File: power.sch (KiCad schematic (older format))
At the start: 19 parts, among them SW5 SW_DPST_NKK_M2021, U13 LM317_SOT223_4pin, U14 LM317_SOT223_4pin

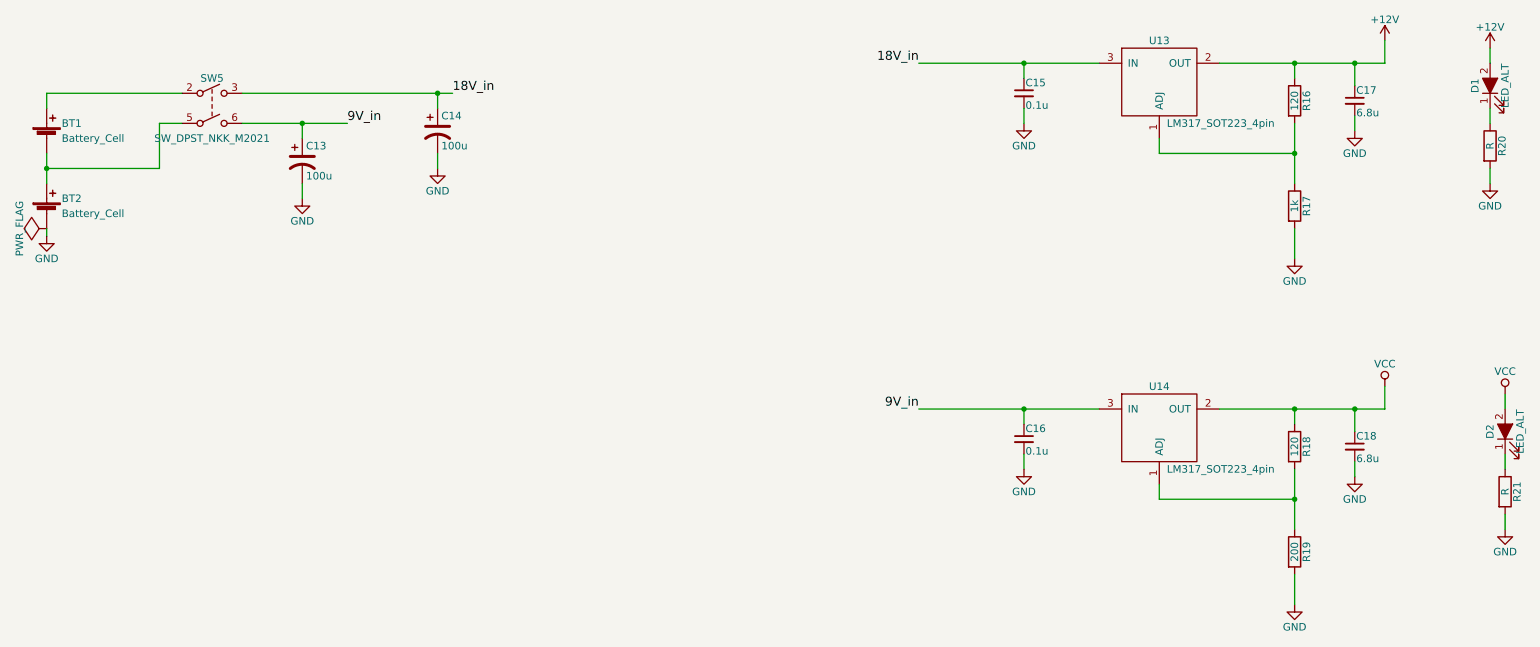
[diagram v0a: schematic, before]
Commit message: Added testpoints for VCC, 12V, and GND
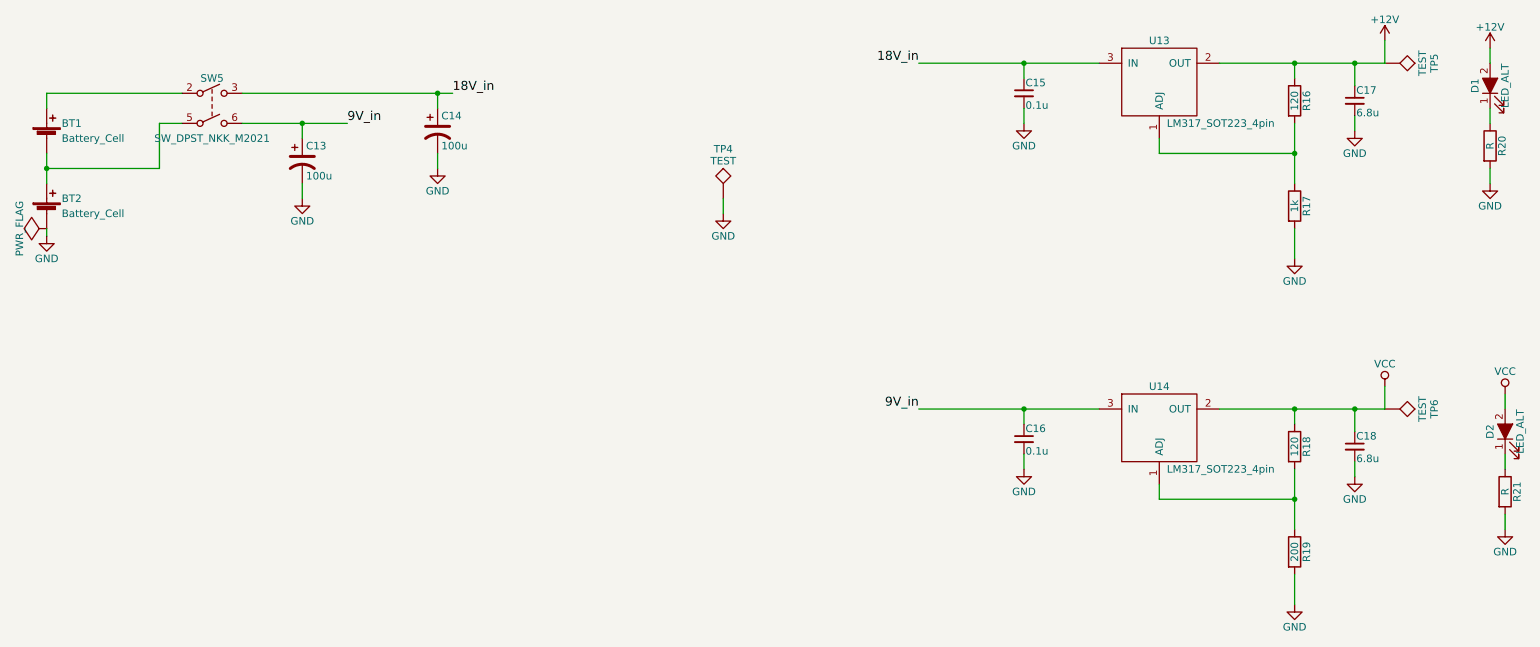
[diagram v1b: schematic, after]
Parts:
- added TP4, TP5, TP6: TEST, Measurement_Points:Measurement_Point_Square-TH_Big, symbol TEST
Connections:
- net +12V: now also TP5.1
- net GND: now also TP4.1
- net VCC: now also TP6.1
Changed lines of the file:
@@
 	1000 2000 1000 2200
 $Comp
-L GND #PWR068
+L GND #PWR069
 U 1 1 58C4B1BE
 P 1000 2550
-F 0 "#PWR068" H 1000 2300 50  0001 C CNN
+F 0 "#PWR069" H 1000 2300 50  0001 C CNN
 F 1 "GND" H 1000 2400 50  0000 C CNN
 F 2 "" H 1000 2550 50  0000 C CNN
@@
 Connection ~ 9300 4300
 $Comp
-L GND #PWR069
+L GND #PWR070
 U 1 1 58C50174
 P 9300 5000
-F 0 "#PWR069" H 9300 4750 50  0001 C CNN
+F 0 "#PWR070" H 9300 4750 50  0001 C CNN
 F 1 "GND" H 9300 4850 50  0000 C CNN
 F 2 "" H 9300 5000 50  0000 C CNN
@@
 $EndComp
 $Comp
-L GND #PWR070
+L GND #PWR071
 U 1 1 58C505E0
 P 7500 4100
-F 0 "#PWR070" H 7500 3850 50  0001 C CNN
+F 0 "#PWR071" H 7500 3850 50  0001 C CNN
 F 1 "GND" H 7500 3950 50  0000 C CNN
 F 2 "" H 7500 4100 50  0000 C CNN
@@
 Connection ~ 7500 3700
 $Comp
-L VCC #PWR071
+L VCC #PWR072
 U 1 1 58C5068E
 P 9900 3550
-F 0 "#PWR071" H 9900 3400 50  0001 C CNN
+F 0 "#PWR072" H 9900 3400 50  0001 C CNN
 F 1 "VCC" H 9900 3700 50  0000 C CNN
 F 2 "" H 9900 3550 50  0000 C CNN
@@
 Connection ~ 9300 3700
 $Comp
-L GND #PWR072
+L GND #PWR073
 U 1 1 58C50749
 P 9700 4150
-F 0 "#PWR072" H 9700 3900 50  0001 C CNN
+F 0 "#PWR073" H 9700 3900 50  0001 C CNN
 F 1 "GND" H 9700 4000 50  0000 C CNN
 F 2 "" H 9700 4150 50  0000 C CNN
@@
 Connection ~ 9300 2000
 $Comp
-L GND #PWR073
+L GND #PWR074
 U 1 1 58C7F4E2
 P 9300 2700
-F 0 "#PWR073" H 9300 2450 50  0001 C CNN
+F 0 "#PWR074" H 9300 2450 50  0001 C CNN
 F 1 "GND" H 9300 2550 50  0000 C CNN
 F 2 "" H 9300 2700 50  0000 C CNN
@@
 $EndComp
 $Comp
-L GND #PWR074
+L GND #PWR075
 U 1 1 58C7F4EF
 P 7500 1800
-F 0 "#PWR074" H 7500 1550 50  0001 C CNN
+F 0 "#PWR075" H 7500 1550 50  0001 C CNN
 F 1 "GND" H 7500 1650 50  0000 C CNN
 F 2 "" H 7500 1800 50  0000 C CNN
@@
 Connection ~ 9300 1400
 $Comp
-L GND #PWR075
+L GND #PWR076
 U 1 1 58C7F506
 P 9700 1850
-F 0 "#PWR075" H 9700 1600 50  0001 C CNN
+F 0 "#PWR076" H 9700 1600 50  0001 C CNN
 F 1 "GND" H 9700 1700 50  0000 C CNN
 F 2 "" H 9700 1850 50  0000 C CNN
@@
 18V_in
 $Comp
-L +12V #PWR076
+L +12V #PWR077
 U 1 1 58C7F582
 P 9900 1250
-F 0 "#PWR076" H 9900 1100 50  0001 C CNN
+F 0 "#PWR077" H 9900 1100 50  0001 C CNN
 F 1 "+12V" H 9900 1390 50  0000 C CNN
 F 2 "" H 9900 1250 50  0000 C CNN
@@
 $EndComp
 $Comp
-L GND #PWR077
+L GND #PWR078
 U 1 1 58C7FF7B
 P 2700 2300
-F 0 "#PWR077" H 2700 2050 50  0001 C CNN
+F 0 "#PWR078" H 2700 2050 50  0001 C CNN
 F 1 "GND" H 2700 2150 50  0000 C CNN
 F 2 "" H 2700 2300 50  0000 C CNN
@@
 $EndComp
 $Comp
-L GND #PWR078
+L GND #PWR079
 U 1 1 58C7FFBA
 P 3600 2100
-F 0 "#PWR078" H 3600 1850 50  0001 C CNN
+F 0 "#PWR079" H 3600 1850 50  0001 C CNN
 F 1 "GND" H 3600 1950 50  0000 C CNN
 F 2 "" H 3600 2100 50  0000 C CNN
@@
 	2700 2300 2700 2200
 $Comp
-L PWR_FLAG #FLG079
+L PWR_FLAG #FLG080
 U 1 1 58C81A82
 P 1000 2500
-F 0 "#FLG079" H 1000 2595 50  0001 C CNN
+F 0 "#FLG080" H 1000 2595 50  0001 C CNN
 F 1 "PWR_FLAG" H 1000 2680 50  0000 C CNN
 F 2 "" H 1000 2500 50  0000 C CNN
@@
 	10600 1700 10600 1800
 $Comp
-L GND #PWR080
+L GND #PWR081
 U 1 1 58C85746
 P 10600 2200
-F 0 "#PWR080" H 10600 1950 50  0001 C CNN
+F 0 "#PWR081" H 10600 1950 50  0001 C CNN
 F 1 "GND" H 10600 2050 50  0000 C CNN
 F 2 "" H 10600 2200 50  0000 C CNN
@@
 	10600 2100 10600 2200
 $Comp
-L +12V #PWR081
+L +12V #PWR082
 U 1 1 58C857D7
 P 10600 1300
-F 0 "#PWR081" H 10600 1150 50  0001 C CNN
+F 0 "#PWR082" H 10600 1150 50  0001 C CNN
 F 1 "+12V" H 10600 1440 50  0000 C CNN
 F 2 "" H 10600 1300 50  0000 C CNN
@@
 	10600 1300 10600 1400
 $Comp
-L GND #PWR082
+L GND #PWR083
 U 1 1 58C85A19
 P 10700 4500
-F 0 "#PWR082" H 10700 4250 50  0001 C CNN
+F 0 "#PWR083" H 10700 4250 50  0001 C CNN
 F 1 "GND" H 10700 4350 50  0000 C CNN
 F 2 "" H 10700 4500 50  0000 C CNN
@@
 	10700 4000 10700 4100
 $Comp
-L VCC #PWR083
+L VCC #PWR084
 U 1 1 58C85C4B
 P 10700 3600
-F 0 "#PWR083" H 10700 3450 50  0001 C CNN
+F 0 "#PWR084" H 10700 3450 50  0001 C CNN
 F 1 "VCC" H 10700 3750 50  0000 C CNN
 F 2 "" H 10700 3600 50  0000 C CNN
@@
 	8800 3700 9900 3700
 Wire Wire Line
-	9900 1400 8800 1400
+	8800 1400 9900 1400
 $Comp
 L SW_DPST_NKK_M2021 SW5
@@
 	1    0    0    -1
 $EndComp
+$Comp
+L TEST TP5
+U 1 1 58C9FA09
+P 9900 1400
+F 0 "TP5" H 9900 1700 50  0000 C BNN
+F 1 "TEST" H 9900 1650 50  0000 C CNN
+F 2 "Measurement_Points:Measurement_Point_Square-TH_Big" H 9900 1400 50  0001 C CNN
+F 3 "" H 9900 1400 50  0000 C CNN
+	1    9900 1400
+	0    1    1    0
+$EndComp
+$Comp
+L TEST TP6
+U 1 1 58C9FB47
+P 9900 3700
+F 0 "TP6" H 9900 4000 50  0000 C BNN
+F 1 "TEST" H 9900 3950 50  0000 C CNN
+F 2 "Measurement_Points:Measurement_Point_Square-TH_Big" H 9900 3700 50  0001 C CNN
+F 3 "" H 9900 3700 50  0000 C CNN
+	1    9900 3700
+	0    1    1    0
+$EndComp
+$Comp
+L TEST TP4
+U 1 1 58C9FE87
+P 5500 2300
+F 0 "TP4" H 5500 2600 50  0000 C BNN
+F 1 "TEST" H 5500 2550 50  0000 C CNN
+F 2 "Measurement_Points:Measurement_Point_Square-TH_Big" H 5500 2300 50  0001 C CNN
+F 3 "" H 5500 2300 50  0000 C CNN
+	1    5500 2300
+	1    0    0    -1
+$EndComp
+$Comp
+L GND #PWR085
+U 1 1 58CA00F3
+P 5500 2400
+F 0 "#PWR085" H 5500 2150 50  0001 C CNN
+F 1 "GND" H 5500 2250 50  0000 C CNN
+F 2 "" H 5500 2400 50  0000 C CNN
+F 3 "" H 5500 2400 50  0000 C CNN
+	1    5500 2400
+	1    0    0    -1
+$EndComp
+Wire Wire Line
+	5500 2300 5500 2400
 $EndSCHEMATC

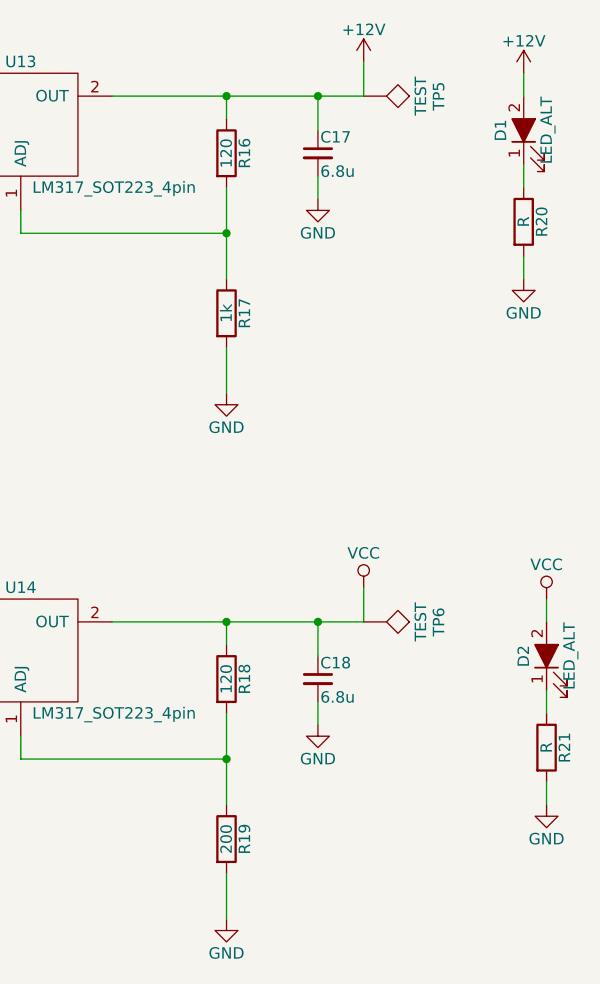
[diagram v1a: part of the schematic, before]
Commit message: Updated voltage output divider to use practical resistor values
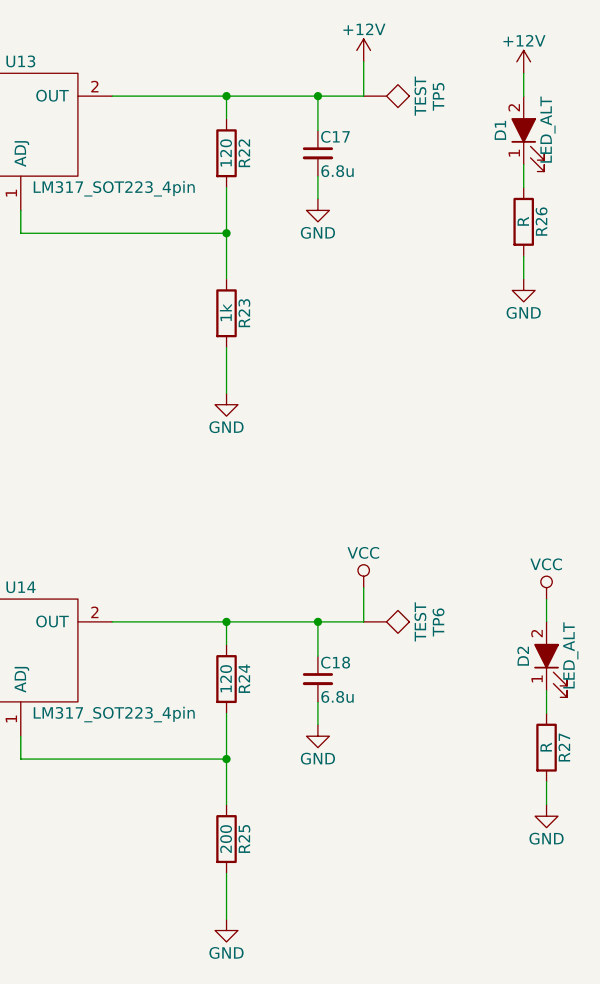
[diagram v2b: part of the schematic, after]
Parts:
- renumbered R16 to R22, R17 to R23, R18 to R24, R19 to R25, R20 to R26, R21 to R27
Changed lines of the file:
@@
 	1000 2000 1000 2200
 $Comp
-L GND #PWR069
+L GND #PWR69
 U 1 1 58C4B1BE
 P 1000 2550
-F 0 "#PWR069" H 1000 2300 50  0001 C CNN
+F 0 "#PWR69" H 1000 2300 50  0001 C CNN
 F 1 "GND" H 1000 2400 50  0000 C CNN
 F 2 "" H 1000 2550 50  0000 C CNN
@@
 Connection ~ 1000 2100
 $Comp
-L R R18
+L R R24
 U 1 1 58C500D3
 P 9300 3950
-F 0 "R18" V 9380 3950 50  0000 C CNN
+F 0 "R24" V 9380 3950 50  0000 C CNN
 F 1 "120" V 9300 3950 50  0000 C CNN
 F 2 "Resistors_SMD:R_0805_HandSoldering" V 9230 3950 50  0001 C CNN
@@
 	8400 4300 8400 4200
 $Comp
-L R R19
+L R R25
 U 1 1 58C50126
 P 9300 4650
-F 0 "R19" V 9380 4650 50  0000 C CNN
+F 0 "R25" V 9380 4650 50  0000 C CNN
 F 1 "200" V 9300 4650 50  0000 C CNN
 F 2 "Resistors_SMD:R_0805_HandSoldering" V 9230 4650 50  0001 C CNN
@@
 Connection ~ 9300 4300
 $Comp
-L GND #PWR070
+L GND #PWR76
 U 1 1 58C50174
 P 9300 5000
-F 0 "#PWR070" H 9300 4750 50  0001 C CNN
+F 0 "#PWR76" H 9300 4750 50  0001 C CNN
 F 1 "GND" H 9300 4850 50  0000 C CNN
 F 2 "" H 9300 5000 50  0000 C CNN
@@
 $EndComp
 $Comp
-L GND #PWR071
+L GND #PWR74
 U 1 1 58C505E0
 P 7500 4100
-F 0 "#PWR071" H 7500 3850 50  0001 C CNN
+F 0 "#PWR74" H 7500 3850 50  0001 C CNN
 F 1 "GND" H 7500 3950 50  0000 C CNN
 F 2 "" H 7500 4100 50  0000 C CNN
@@
 Connection ~ 7500 3700
 $Comp
-L VCC #PWR072
+L VCC #PWR80
 U 1 1 58C5068E
 P 9900 3550
-F 0 "#PWR072" H 9900 3400 50  0001 C CNN
+F 0 "#PWR80" H 9900 3400 50  0001 C CNN
 F 1 "VCC" H 9900 3700 50  0000 C CNN
 F 2 "" H 9900 3550 50  0000 C CNN
@@
 Connection ~ 9300 3700
 $Comp
-L GND #PWR073
+L GND #PWR78
 U 1 1 58C50749
 P 9700 4150
-F 0 "#PWR073" H 9700 3900 50  0001 C CNN
+F 0 "#PWR78" H 9700 3900 50  0001 C CNN
 F 1 "GND" H 9700 4000 50  0000 C CNN
 F 2 "" H 9700 4150 50  0000 C CNN
@@
 	1750 1800 1900 1800
 $Comp
-L R R16
+L R R22
 U 1 1 58C7F4D0
 P 9300 1650
-F 0 "R16" V 9380 1650 50  0000 C CNN
+F 0 "R22" V 9380 1650 50  0000 C CNN
 F 1 "120" V 9300 1650 50  0000 C CNN
 F 2 "Resistors_SMD:R_0805_HandSoldering" V 9230 1650 50  0001 C CNN
@@
 	8400 2000 8400 1900
 $Comp
-L R R17
+L R R23
 U 1 1 58C7F4DB
 P 9300 2350
-F 0 "R17" V 9380 2350 50  0000 C CNN
+F 0 "R23" V 9380 2350 50  0000 C CNN
 F 1 "1k" V 9300 2350 50  0000 C CNN
 F 2 "Resistors_SMD:R_0805_HandSoldering" V 9230 2350 50  0001 C CNN
@@
 Connection ~ 9300 2000
 $Comp
-L GND #PWR074
+L GND #PWR75
 U 1 1 58C7F4E2
 P 9300 2700
-F 0 "#PWR074" H 9300 2450 50  0001 C CNN
+F 0 "#PWR75" H 9300 2450 50  0001 C CNN
 F 1 "GND" H 9300 2550 50  0000 C CNN
 F 2 "" H 9300 2700 50  0000 C CNN
@@
 $EndComp
 $Comp
-L GND #PWR075
+L GND #PWR73
 U 1 1 58C7F4EF
 P 7500 1800
-F 0 "#PWR075" H 7500 1550 50  0001 C CNN
+F 0 "#PWR73" H 7500 1550 50  0001 C CNN
 F 1 "GND" H 7500 1650 50  0000 C CNN
 F 2 "" H 7500 1800 50  0000 C CNN
@@
 Connection ~ 9300 1400
 $Comp
-L GND #PWR076
+L GND #PWR77
 U 1 1 58C7F506
 P 9700 1850
-F 0 "#PWR076" H 9700 1600 50  0001 C CNN
+F 0 "#PWR77" H 9700 1600 50  0001 C CNN
 F 1 "GND" H 9700 1700 50  0000 C CNN
 F 2 "" H 9700 1850 50  0000 C CNN
@@
 18V_in
 $Comp
-L +12V #PWR077
+L +12V #PWR79
 U 1 1 58C7F582
 P 9900 1250
-F 0 "#PWR077" H 9900 1100 50  0001 C CNN
+F 0 "#PWR79" H 9900 1100 50  0001 C CNN
 F 1 "+12V" H 9900 1390 50  0000 C CNN
 F 2 "" H 9900 1250 50  0000 C CNN
@@
 $EndComp
 $Comp
-L GND #PWR078
+L GND #PWR70
 U 1 1 58C7FF7B
 P 2700 2300
-F 0 "#PWR078" H 2700 2050 50  0001 C CNN
+F 0 "#PWR70" H 2700 2050 50  0001 C CNN
 F 1 "GND" H 2700 2150 50  0000 C CNN
 F 2 "" H 2700 2300 50  0000 C CNN
@@
 $EndComp
 $Comp
-L GND #PWR079
+L GND #PWR71
 U 1 1 58C7FFBA
 P 3600 2100
-F 0 "#PWR079" H 3600 1850 50  0001 C CNN
+F 0 "#PWR71" H 3600 1850 50  0001 C CNN
 F 1 "GND" H 3600 1950 50  0000 C CNN
 F 2 "" H 3600 2100 50  0000 C CNN
@@
 	2700 2300 2700 2200
 $Comp
-L PWR_FLAG #FLG080
+L PWR_FLAG #FLG1
 U 1 1 58C81A82
 P 1000 2500
-F 0 "#FLG080" H 1000 2595 50  0001 C CNN
+F 0 "#FLG1" H 1000 2595 50  0001 C CNN
 F 1 "PWR_FLAG" H 1000 2680 50  0000 C CNN
 F 2 "" H 1000 2500 50  0000 C CNN
@@
 $EndComp
 $Comp
-L R R21
+L R R27
 U 1 1 58C8554B
 P 10700 4250
-F 0 "R21" V 10780 4250 50  0000 C CNN
+F 0 "R27" V 10780 4250 50  0000 C CNN
 F 1 "R" V 10700 4250 50  0000 C CNN
 F 2 "Resistors_SMD:R_0805_HandSoldering" V 10630 4250 50  0001 C CNN
@@
 $EndComp
 $Comp
-L R R20
+L R R26
 U 1 1 58C855B8
 P 10600 1950
-F 0 "R20" V 10680 1950 50  0000 C CNN
+F 0 "R26" V 10680 1950 50  0000 C CNN
 F 1 "R" V 10600 1950 50  0000 C CNN
 F 2 "Resistors_SMD:R_0805_HandSoldering" V 10530 1950 50  0001 C CNN
@@
 	10600 1700 10600 1800
 $Comp
-L GND #PWR081
+L GND #PWR82
 U 1 1 58C85746
 P 10600 2200
-F 0 "#PWR081" H 10600 1950 50  0001 C CNN
+F 0 "#PWR82" H 10600 1950 50  0001 C CNN
 F 1 "GND" H 10600 2050 50  0000 C CNN
 F 2 "" H 10600 2200 50  0000 C CNN
@@
 	10600 2100 10600 2200
 $Comp
-L +12V #PWR082
+L +12V #PWR81
 U 1 1 58C857D7
 P 10600 1300
-F 0 "#PWR082" H 10600 1150 50  0001 C CNN
+F 0 "#PWR81" H 10600 1150 50  0001 C CNN
 F 1 "+12V" H 10600 1440 50  0000 C CNN
 F 2 "" H 10600 1300 50  0000 C CNN
@@
 	10600 1300 10600 1400
 $Comp
-L GND #PWR083
+L GND #PWR84
 U 1 1 58C85A19
 P 10700 4500
-F 0 "#PWR083" H 10700 4250 50  0001 C CNN
+F 0 "#PWR84" H 10700 4250 50  0001 C CNN
 F 1 "GND" H 10700 4350 50  0000 C CNN
 F 2 "" H 10700 4500 50  0000 C CNN
@@
 	10700 4000 10700 4100
 $Comp
-L VCC #PWR084
+L VCC #PWR83
 U 1 1 58C85C4B
 P 10700 3600
-F 0 "#PWR084" H 10700 3450 50  0001 C CNN
+F 0 "#PWR83" H 10700 3450 50  0001 C CNN
 F 1 "VCC" H 10700 3750 50  0000 C CNN
 F 2 "" H 10700 3600 50  0000 C CNN
@@
 $EndComp
 $Comp
-L GND #PWR085
+L GND #PWR72
 U 1 1 58CA00F3
 P 5500 2400
-F 0 "#PWR085" H 5500 2150 50  0001 C CNN
+F 0 "#PWR72" H 5500 2150 50  0001 C CNN
 F 1 "GND" H 5500 2250 50  0000 C CNN
 F 2 "" H 5500 2400 50  0000 C CNN
